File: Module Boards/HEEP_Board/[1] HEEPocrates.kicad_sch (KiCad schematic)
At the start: 20 parts, among them U2 HEEPocrates, U3 SIT1532AC-J5-DCC-32.768D

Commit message: Fixed path dependencies and changed library name to X-MODs
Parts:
- C1, C10, C11, C12, C13, C14, C2, C3, C4, C5, C6, C7, C8, C9: footprint HeepoMind_PcbLib:C0402 -> X-MODs_PcbLib:C0402; symbol HeepoMind_SchLib:GRM155R71A104JA01D -> X-MODs_SchLib:GRM155R71A104JA01D
- R1: footprint HeepoMind_PcbLib:R0402 -> X-MODs_PcbLib:R0402; symbol HeepoMind_SchLib:CRCW0402100KFKEDC -> X-MODs_SchLib:CRCW0402100KFKEDC
- R2, R3: footprint HeepoMind_PcbLib:R0402 -> X-MODs_PcbLib:R0402; symbol HeepoMind_SchLib:CRCW040210K0FKEDHP -> X-MODs_SchLib:CRCW040210K0FKEDHP
- U1: footprint HeepoMind_PcbLib:X2SON-6 -> X-MODs_PcbLib:X2SON-6; symbol HeepoMind_SchLib:SN74AUP1G14DSFR -> X-MODs_SchLib:SN74AUP1G14DSFR
- U2: footprint HeepoMind_PcbLib:HEEPocrates -> X-MODs_PcbLib:HEEPocrates; symbol HeepoMind_SchLib:HEEPocrates -> X-MODs_SchLib:HEEPocrates
- U3: footprint HeepoMind_PcbLib:SIT1532AC -> X-MODs_PcbLib:SIT1532AC; symbol HeepoMind_SchLib:SIT1532AC-J5-DCC-32.768D -> X-MODs_SchLib:SIT1532AC-J5-DCC-32.768D
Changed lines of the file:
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@@
 	)
 	(symbol
-		(lib_id "HeepoMind_SchLib:GRM155R71A104JA01D")
+		(lib_id "X-MODs_SchLib:GRM155R71A104JA01D")
 		(at 217.17 34.29 90)
 		(unit 1)
@@
 			)
 		)
-		(property "Footprint" "HeepoMind_PcbLib:C0402"
+		(property "Footprint" "X-MODs_PcbLib:C0402"
 			(at 225.806 71.374 0)
 			(effects
@@
 	)
 	(symbol
-		(lib_id "HeepoMind_SchLib:CRCW040210K0FKEDHP")
+		(lib_id "X-MODs_SchLib:CRCW040210K0FKEDHP")
 		(at 72.39 114.3 270)
 		(unit 1)
@@
 			)
 		)
-		(property "Footprint" "HeepoMind_PcbLib:R0402"
+		(property "Footprint" "X-MODs_PcbLib:R0402"
 			(at 69.088 99.314 0)
 			(effects
@@
 	)
 	(symbol
-		(lib_id "HeepoMind_SchLib:HEEPocrates")
+		(lib_id "X-MODs_SchLib:HEEPocrates")
 		(at 106.68 36.83 0)
 		(unit 1)
@@
 			)
 		)
-		(property "Footprint" "HeepoMind_PcbLib:HEEPocrates"
+		(property "Footprint" "X-MODs_PcbLib:HEEPocrates"
 			(at 135.636 181.102 0)
 			(effects
@@
 	)
 	(symbol
-		(lib_id "HeepoMind_SchLib:GRM155R71A104JA01D")
+		(lib_id "X-MODs_SchLib:GRM155R71A104JA01D")
 		(at 81.28 34.29 90)
 		(unit 1)
@@
 			)
 		)
-		(property "Footprint" "HeepoMind_PcbLib:C0402"
+		(property "Footprint" "X-MODs_PcbLib:C0402"
 			(at 89.916 71.374 0)
 			(effects
@@
 	)
 	(symbol
-		(lib_id "HeepoMind_SchLib:GRM155R71A104JA01D")
+		(lib_id "X-MODs_SchLib:GRM155R71A104JA01D")
 		(at 91.44 34.29 90)
 		(unit 1)
@@
 			)
 		)
-		(property "Footprint" "HeepoMind_PcbLib:C0402"
+		(property "Footprint" "X-MODs_PcbLib:C0402"
 			(at 100.076 71.374 0)
 			(effects
@@
 	)
 	(symbol
-		(lib_id "HeepoMind_SchLib:CRCW0402100KFKEDC")
+		(lib_id "X-MODs_SchLib:CRCW0402100KFKEDC")
 		(at 255.27 62.23 270)
 		(unit 1)
@@
 			)
 		)
-		(property "Footprint" "HeepoMind_PcbLib:R0402"
+		(property "Footprint" "X-MODs_PcbLib:R0402"
 			(at 251.968 47.244 0)
 			(effects
@@
 	)
 	(symbol
-		(lib_id "HeepoMind_SchLib:GRM155R71A104JA01D")
+		(lib_id "X-MODs_SchLib:GRM155R71A104JA01D")
 		(at 237.49 34.29 90)
 		(unit 1)
@@
 			)
 		)
-		(property "Footprint" "HeepoMind_PcbLib:C0402"
+		(property "Footprint" "X-MODs_PcbLib:C0402"
 			(at 246.126 71.374 0)
 			(effects
@@
 	)
 	(symbol
-		(lib_id "HeepoMind_SchLib:GRM155R71A104JA01D")
+		(lib_id "X-MODs_SchLib:GRM155R71A104JA01D")
 		(at 222.25 34.29 90)
 		(unit 1)
@@
 			)
 		)
-		(property "Footprint" "HeepoMind_PcbLib:C0402"
+		(property "Footprint" "X-MODs_PcbLib:C0402"
 			(at 230.886 71.374 0)
 			(effects
@@
 	)
 	(symbol
-		(lib_id "HeepoMind_SchLib:CRCW040210K0FKEDHP")
+		(lib_id "X-MODs_SchLib:CRCW040210K0FKEDHP")
 		(at 62.23 114.3 270)
 		(unit 1)
@@
 			)
 		)
-		(property "Footprint" "HeepoMind_PcbLib:R0402"
+		(property "Footprint" "X-MODs_PcbLib:R0402"
 			(at 58.928 99.314 0)
 			(effects
@@
 	)
 	(symbol
-		(lib_id "HeepoMind_SchLib:GRM155R71A104JA01D")
+		(lib_id "X-MODs_SchLib:GRM155R71A104JA01D")
 		(at 259.08 34.29 90)
 		(unit 1)
@@
 			)
 		)
-		(property "Footprint" "HeepoMind_PcbLib:C0402"
+		(property "Footprint" "X-MODs_PcbLib:C0402"
 			(at 267.716 71.374 0)
 			(effects
@@
 	)
 	(symbol
-		(lib_id "HeepoMind_SchLib:GRM155R71A104JA01D")
+		(lib_id "X-MODs_SchLib:GRM155R71A104JA01D")
 		(at 212.09 34.29 90)
 		(unit 1)
@@
 			)
 		)
-		(property "Footprint" "HeepoMind_PcbLib:C0402"
+		(property "Footprint" "X-MODs_PcbLib:C0402"
 			(at 220.726 71.374 0)
 			(effects
@@
 	)
 	(symbol
-		(lib_id "HeepoMind_SchLib:GRM155R71A104JA01D")
+		(lib_id "X-MODs_SchLib:GRM155R71A104JA01D")
 		(at 76.2 34.29 90)
 		(unit 1)
@@
 			)
 		)
-		(property "Footprint" "HeepoMind_PcbLib:C0402"
+		(property "Footprint" "X-MODs_PcbLib:C0402"
 			(at 84.836 71.374 0)
 			(effects
@@
 	)
 	(symbol
-		(lib_id "HeepoMind_SchLib:GRM155R71A104JA01D")
+		(lib_id "X-MODs_SchLib:GRM155R71A104JA01D")
 		(at 227.33 34.29 90)
 		(unit 1)
@@
 			)
 		)
-		(property "Footprint" "HeepoMind_PcbLib:C0402"
+		(property "Footprint" "X-MODs_PcbLib:C0402"
 			(at 235.966 71.374 0)
 			(effects
@@
 	)
 	(symbol
-		(lib_id "HeepoMind_SchLib:GRM155R71A104JA01D")
+		(lib_id "X-MODs_SchLib:GRM155R71A104JA01D")
 		(at 31.75 63.5 90)
 		(unit 1)
@@
 			)
 		)
-		(property "Footprint" "HeepoMind_PcbLib:C0402"
+		(property "Footprint" "X-MODs_PcbLib:C0402"
 			(at 40.386 100.584 0)
 			(effects
@@
 	)
 	(symbol
-		(lib_id "HeepoMind_SchLib:GRM155R71A104JA01D")
+		(lib_id "X-MODs_SchLib:GRM155R71A104JA01D")
 		(at 96.52 34.29 90)
 		(unit 1)
@@
 			)
 		)
-		(property "Footprint" "HeepoMind_PcbLib:C0402"
+		(property "Footprint" "X-MODs_PcbLib:C0402"
 			(at 105.156 71.374 0)
 			(effects
@@
 	)
 	(symbol
-		(lib_id "HeepoMind_SchLib:GRM155R71A104JA01D")
+		(lib_id "X-MODs_SchLib:GRM155R71A104JA01D")
 		(at 71.12 34.29 90)
 		(unit 1)
@@
 			)
 		)
-		(property "Footprint" "HeepoMind_PcbLib:C0402"
+		(property "Footprint" "X-MODs_PcbLib:C0402"
 			(at 79.756 71.374 0)
 			(effects
@@
 	)
 	(symbol
-		(lib_id "HeepoMind_SchLib:SN74AUP1G14DSFR")
+		(lib_id "X-MODs_SchLib:SN74AUP1G14DSFR")
 		(at 271.78 26.67 0)
 		(unit 2)
@@
 			)
 		)
-		(property "Footprint" "HeepoMind_PcbLib:X2SON-6"
+		(property "Footprint" "X-MODs_PcbLib:X2SON-6"
 			(at 276.098 34.29 0)
 			(effects
@@
 	)
 	(symbol
-		(lib_id "HeepoMind_SchLib:SN74AUP1G14DSFR")
+		(lib_id "X-MODs_SchLib:SN74AUP1G14DSFR")
 		(at 250.19 53.34 0)
 		(mirror y)
@@
 			)
 		)
-		(property "Footprint" "HeepoMind_PcbLib:X2SON-6"
+		(property "Footprint" "X-MODs_PcbLib:X2SON-6"
 			(at 245.872 60.96 0)
 			(effects
@@
 	)
 	(symbol
-		(lib_id "HeepoMind_SchLib:SIT1532AC-J5-DCC-32.768D")
+		(lib_id "X-MODs_SchLib:SIT1532AC-J5-DCC-32.768D")
 		(at 44.45 55.88 0)
 		(unit 1)
@@
 			)
 		)
-		(property "Footprint" "HeepoMind_PcbLib:SIT1532AC"
+		(property "Footprint" "X-MODs_PcbLib:SIT1532AC"
 			(at 44.45 71.12 0)
 			(effects
@@
 	)
 	(symbol
-		(lib_id "HeepoMind_SchLib:GRM155R71A104JA01D")
+		(lib_id "X-MODs_SchLib:GRM155R71A104JA01D")
 		(at 86.36 34.29 90)
 		(unit 1)
@@
 			)
 		)
-		(property "Footprint" "HeepoMind_PcbLib:C0402"
+		(property "Footprint" "X-MODs_PcbLib:C0402"
 			(at 94.996 71.374 0)
 			(effects
@@
 	)
 	(symbol
-		(lib_id "HeepoMind_SchLib:GRM155R71A104JA01D")
+		(lib_id "X-MODs_SchLib:GRM155R71A104JA01D")
 		(at 232.41 34.29 90)
 		(unit 1)
@@
 			)
 		)
-		(property "Footprint" "HeepoMind_PcbLib:C0402"
+		(property "Footprint" "X-MODs_PcbLib:C0402"
 			(at 241.046 71.374 0)
 			(effects

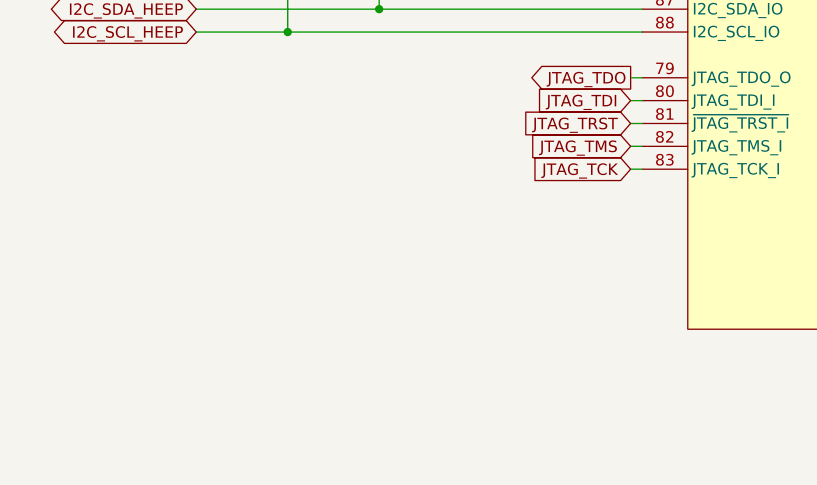
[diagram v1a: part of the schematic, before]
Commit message: Added ADC to board and partially placed/routed the updated board
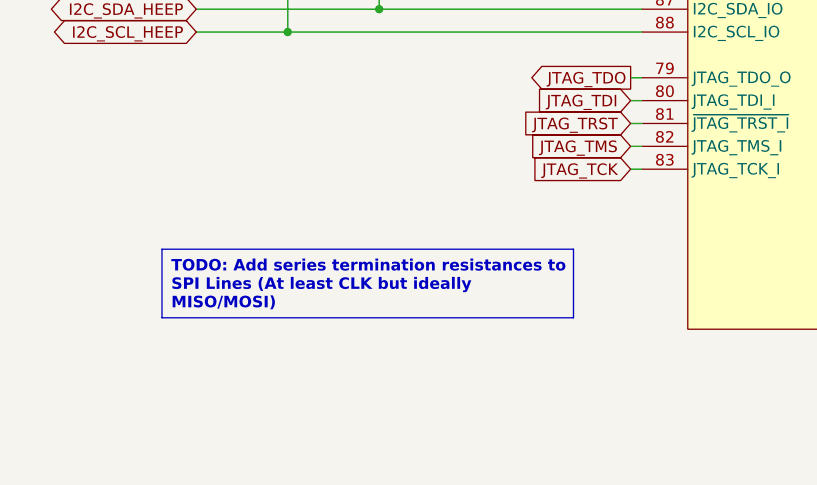
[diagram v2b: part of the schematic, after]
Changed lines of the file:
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@@
+		)
+	)
+	(text_box "TODO: Add series termination resistances to SPI Lines (At least CLK but ideally MISO/MOSI)"
+		(exclude_from_sim no)
+		(at 48.26 148.59 0)
+		(size 45.72 7.62)
+		(stroke
+			(width 0)
+			(type default)
+		)
+		(fill
+			(type color)
+			(color 255 255 150 1)
+		)
+		(effects
+			(font
+				(size 1.27 1.27)
+				(thickness 0.254)
+				(bold yes)
+				(color 255 2 0 1)
+			)
+			(justify left top)
 		)
 	)
